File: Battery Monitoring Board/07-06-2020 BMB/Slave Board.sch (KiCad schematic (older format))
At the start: 64 parts, among them IC1 LTC6820IMS#PBF, IC2 LTC6804-2, J1 Conn_01x02, J10 Conn_01x02, J11 Conn_01x02, J12 Conn_01x02, J13 Conn_01x06, J2 Conn_01x02, J26 Conn_01x01, J27 Conn_01x04, J3 Conn_01x02, J4 Conn_01x02, J5 Conn_01x02, J6 Conn_01x02, J7 Conn_01x02, J8 Conn_01x02, J9 Conn_01x02, Q1 Q_NPN_BCE, T1 PE-68386NL, U1 MCP2551_CANmodule, U2 MCP2551-I-SN, U3 OKI-78SR-3.3_1.5-W36-C, U4 ISO1050DUB, U5 TMR_1-1212, U6 ARDUINO_MICRO_SHIELD

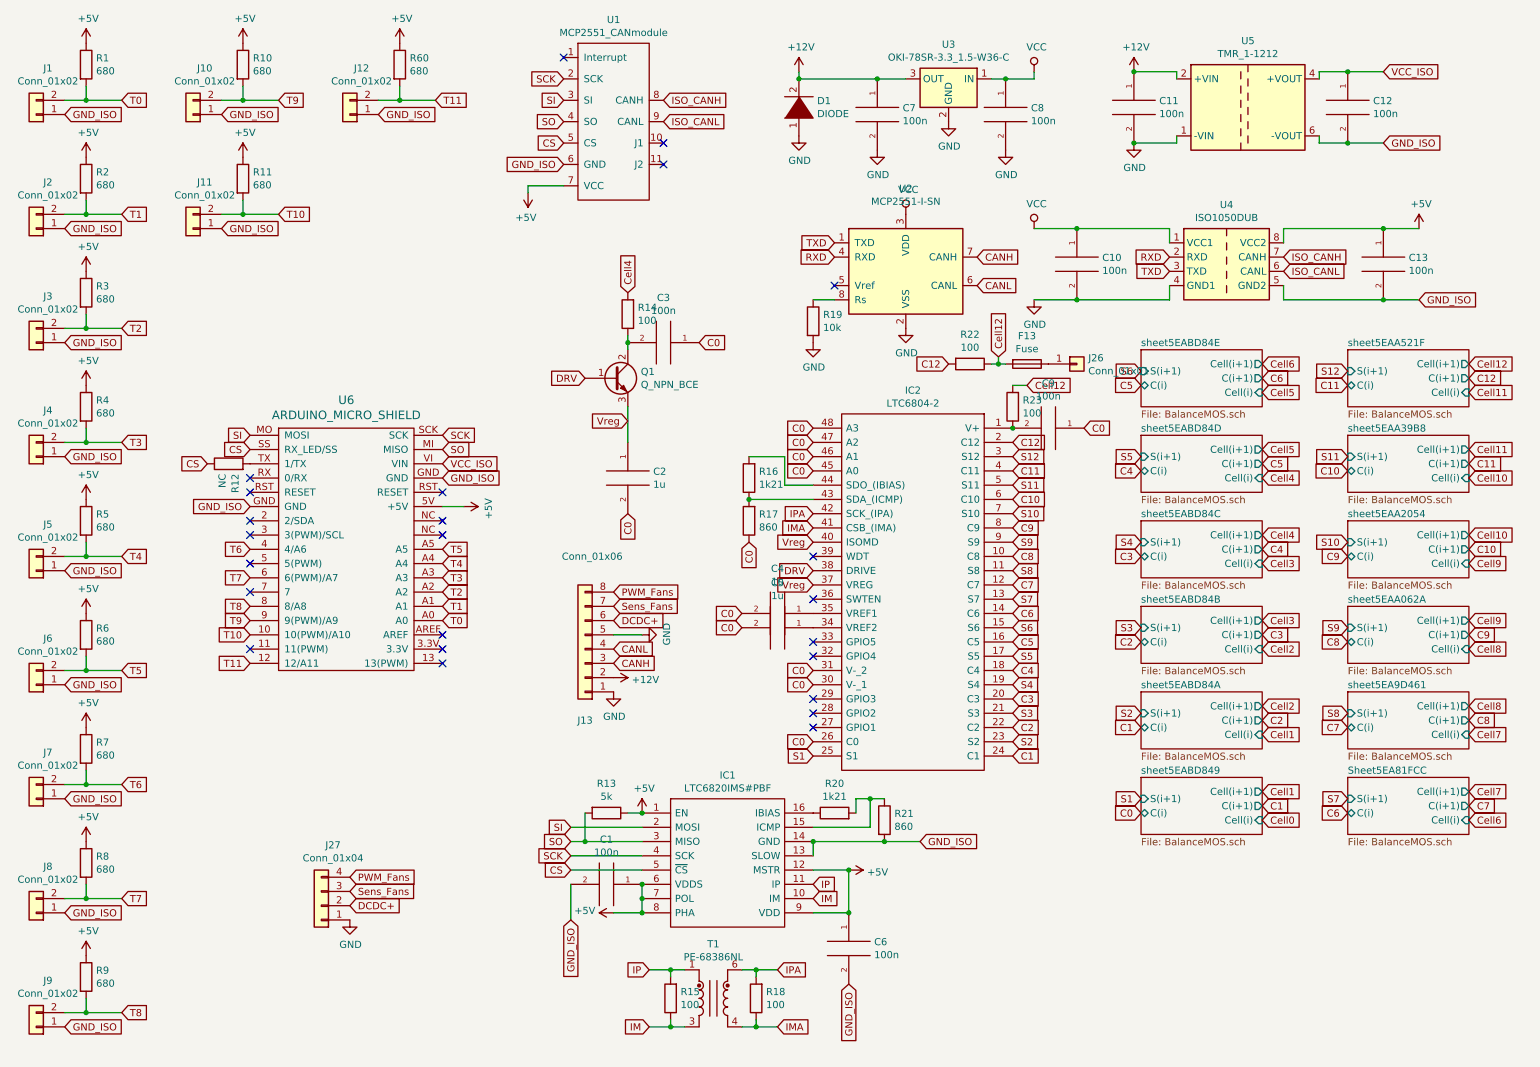
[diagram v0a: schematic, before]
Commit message: BMB wired BMI connector
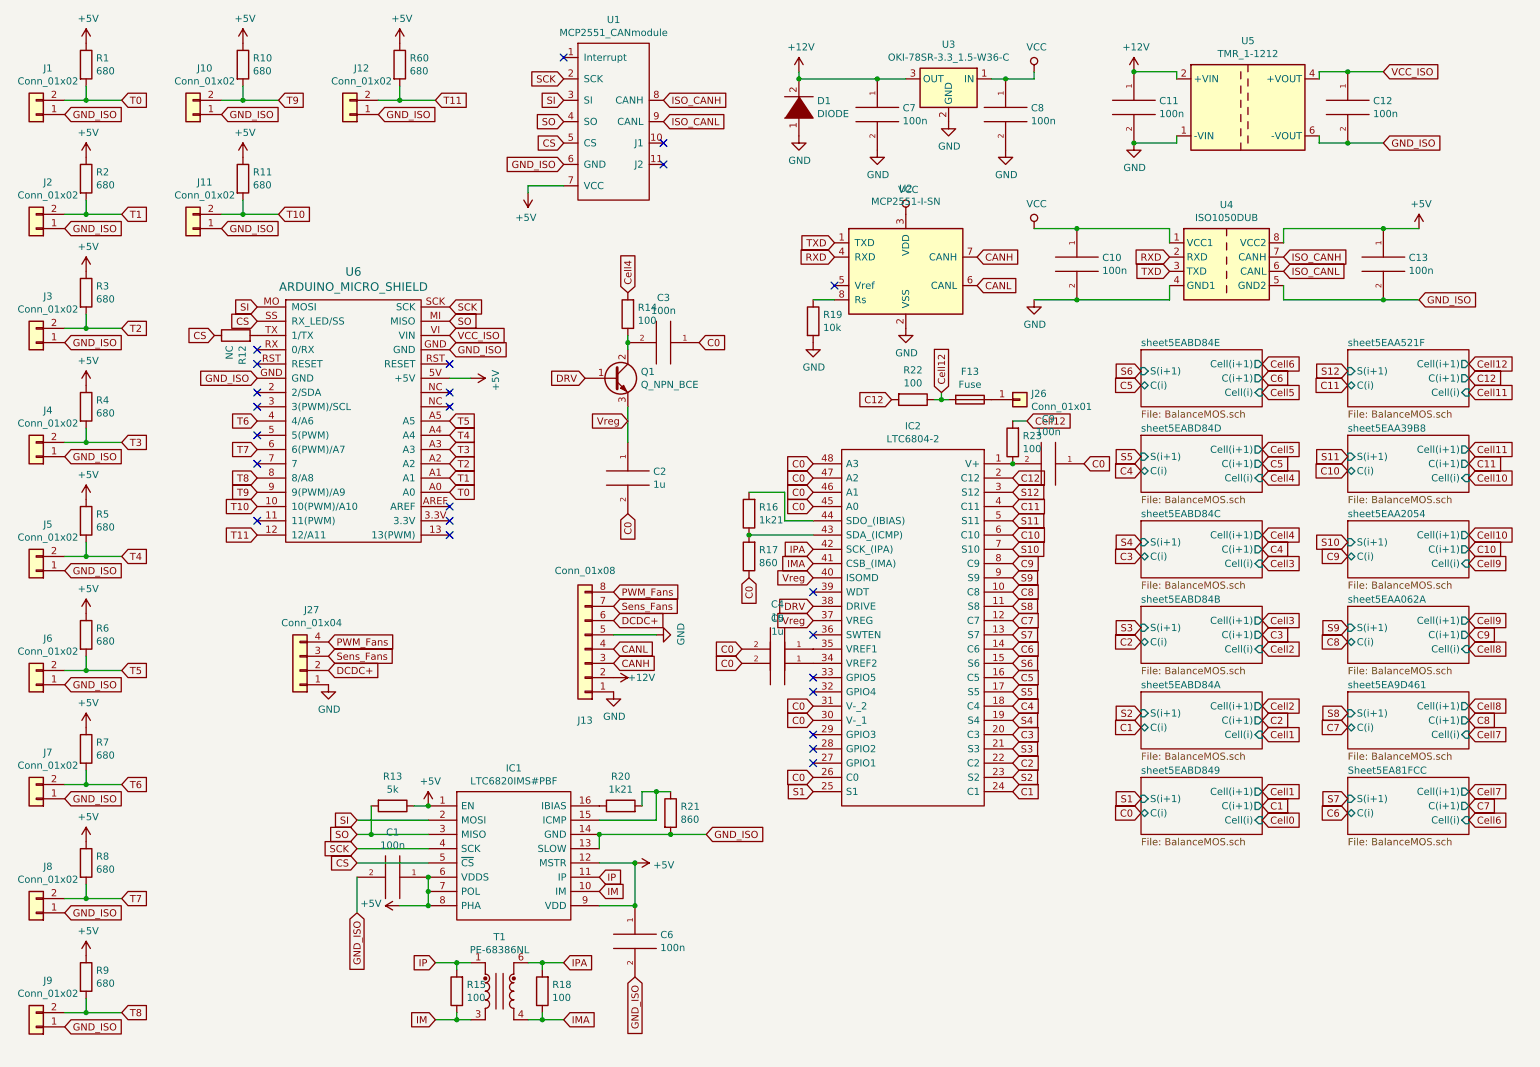
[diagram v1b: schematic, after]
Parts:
- J13: value Conn_01x06 -> Conn_01x08; footprint 44764-0802:447640802 -> Connector_Molex:Molex_Micro-Fit_3.0_43045-0800_2x04_P3.00mm_Horizontal
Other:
- moved on the sheet: C1, C4, C5, C6, C9, F13, IC1, IC2, J26, J27, R12, R13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
